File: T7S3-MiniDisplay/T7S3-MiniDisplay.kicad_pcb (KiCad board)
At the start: 2 copper layers, 67.3 x 63.5 mm, 30 parts, among them J101 Qwicc, J102 Micro_SD_Card_Det, J801 RJ45, J802 RJ45, T801 - 15 in +, T802 - 15 out +, U101 TTGO-T7_S3-V1.1, U301 AP63205, U801 TCAN332DR

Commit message: Minor updates.
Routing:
- net /SDA: track 57.0 -> 49.8 mm
- net /SCL: track 65.3 -> 62.5 mm
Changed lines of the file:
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@@
   (segment (start 108.877 91.1255) (end 108.959 91.2075) (width 0.8) (layer "F.Cu") (net 35))
   (segment (start 108.877 84.582) (end 108.877 91.1255) (width 0.8) (layer "F.Cu") (net 35))
-  (segment (start 103.025685 53.914) (end 103.632 53.307685) (width 0.2) (layer "F.Cu") (net 36))
-  (segment (start 103.632 53.307685) (end 103.632 50.0595) (width 0.2) (layer "F.Cu") (net 36))
+  (segment (start 103.632 53.307685) (end 103.025685 53.914) (width 0.2) (layer "F.Cu") (net 36))
   (segment (start 123.698 52.07) (end 123.698 37.338) (width 0.2) (layer "F.Cu") (net 36))
+  (segment (start 103.632 52.07) (end 103.632 53.307685) (width 0.2) (layer "F.Cu") (net 36))
   (segment (start 123.698 37.338) (end 123.444 37.084) (width 0.2) (layer "F.Cu") (net 36))
-  (segment (start 102.87 53.914) (end 103.025685 53.914) (width 0.2) (layer "F.Cu") (net 36))
+  (segment (start 103.025685 53.914) (end 102.87 53.914) (width 0.2) (layer "F.Cu") (net 36))
   (segment (start 102.796 53.84) (end 102.87 53.914) (width 0.2) (layer "F.Cu") (net 36))
   (segment (start 101.06 53.84) (end 102.796 53.84) (width 0.2) (layer "F.Cu") (net 36))
   (via (at 123.444 37.084) (size 0.8) (drill 0.4) (layers "F.Cu" "B.Cu") (net 36))
   (via (at 123.698 52.07) (size 0.8) (drill 0.4) (layers "F.Cu" "B.Cu") (net 36))
-  (via (at 103.632 50.0595) (size 0.8) (drill 0.4) (layers "F.Cu" "B.Cu") (net 36))
+  (via (at 103.632 52.07) (size 0.8) (drill 0.4) (layers "F.Cu" "B.Cu") (net 36))
   (segment (start 123.698 36.83) (end 144.78 36.83) (width 0.2) (layer "B.Cu") (net 36))
   (segment (start 144.78 36.83) (end 146.05 35.56) (width 0.2) (layer "B.Cu") (net 36))
   (segment (start 123.444 37.084) (end 123.698 36.83) (width 0.2) (layer "B.Cu") (net 36))
-  (segment (start 103.632 50.0595) (end 105.6425 52.07) (width 0.2) (layer "B.Cu") (net 36))
-  (segment (start 105.6425 52.07) (end 123.698 52.07) (width 0.2) (layer "B.Cu") (net 36))
-  (segment (start 98.552 53.34) (end 100.052 54.84) (width 0.2) (layer "F.Cu") (net 37))
+  (segment (start 103.632 52.07) (end 123.698 52.07) (width 0.2) (layer "B.Cu") (net 36))
+  (segment (start 105.300767 49.36) (end 105.300767 52.530233) (width 0.2) (layer "F.Cu") (net 37))
+  (segment (start 105.300767 52.530233) (end 102.87 54.961) (width 0.2) (layer "F.Cu") (net 37))
   (segment (start 101.06 54.84) (end 102.749 54.84) (width 0.2) (layer "F.Cu") (net 37))
-  (segment (start 98.722 49.36) (end 98.552 49.53) (width 0.2) (layer "F.Cu") (net 37))
   (segment (start 102.749 54.84) (end 102.87 54.961) (width 0.2) (layer "F.Cu") (net 37))
-  (segment (start 100.052 54.84) (end 101.06 54.84) (width 0.2) (layer "F.Cu") (net 37))
-  (segment (start 98.552 49.53) (end 98.552 53.34) (width 0.2) (layer "F.Cu") (net 37))
-  (via (at 98.722 49.36) (size 0.8) (drill 0.4) (layers "F.Cu" "B.Cu") (net 37))
+  (via (at 105.300767 49.36) (size 0.8) (drill 0.4) (layers "F.Cu" "B.Cu") (net 37))
+  (segment (start 105.300767 49.36) (end 144.61 49.36) (width 0.2) (layer "B.Cu") (net 37))
   (segment (start 144.61 49.36) (end 146.05 50.8) (width 0.2) (layer "B.Cu") (net 37))
-  (segment (start 98.722 49.36) (end 144.61 49.36) (width 0.2) (layer "B.Cu") (net 37))
   (segment (start 114.249487 33.788513) (end 114.134 33.904) (width 0.2) (layer "F.Cu") (net 38))
   (segment (start 116.332 36.322) (end 116.332 35.052) (width 0.2) (layer "F.Cu") (net 38))

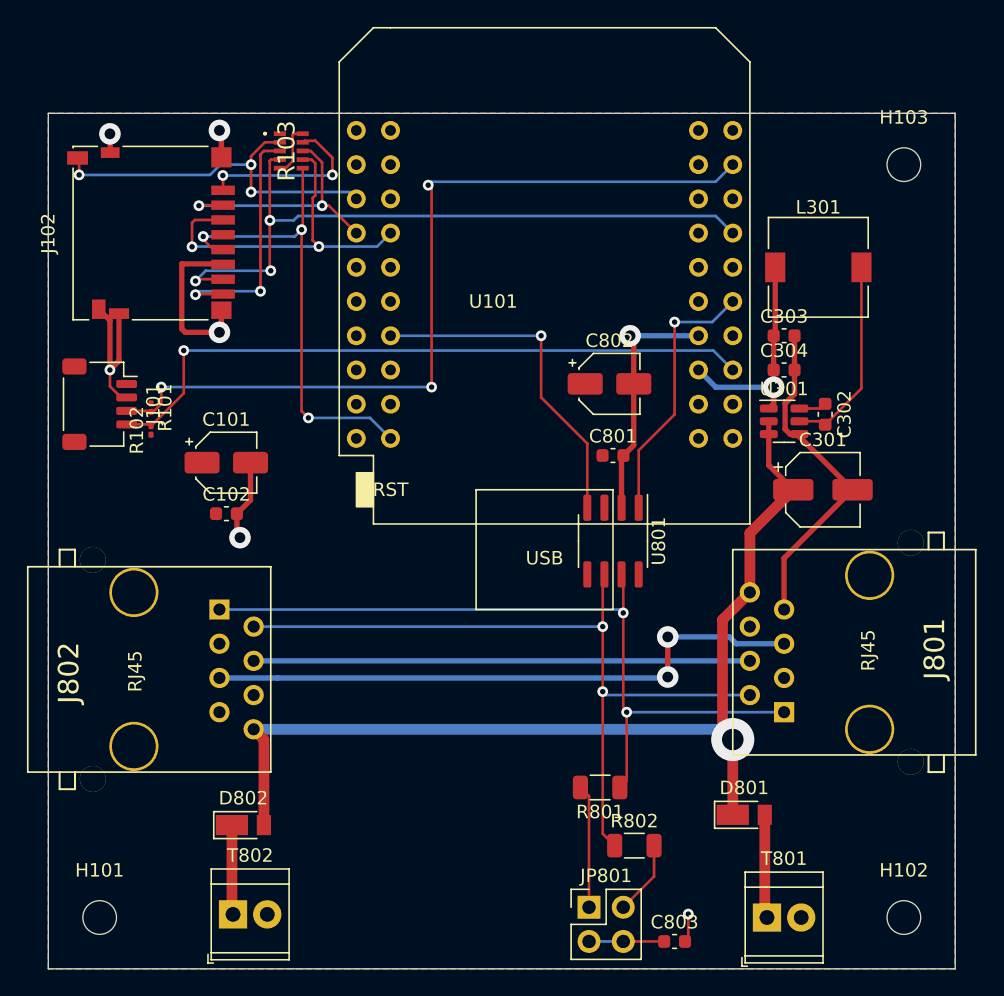
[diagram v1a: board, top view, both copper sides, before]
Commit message: Clean up PCB silkscreen.
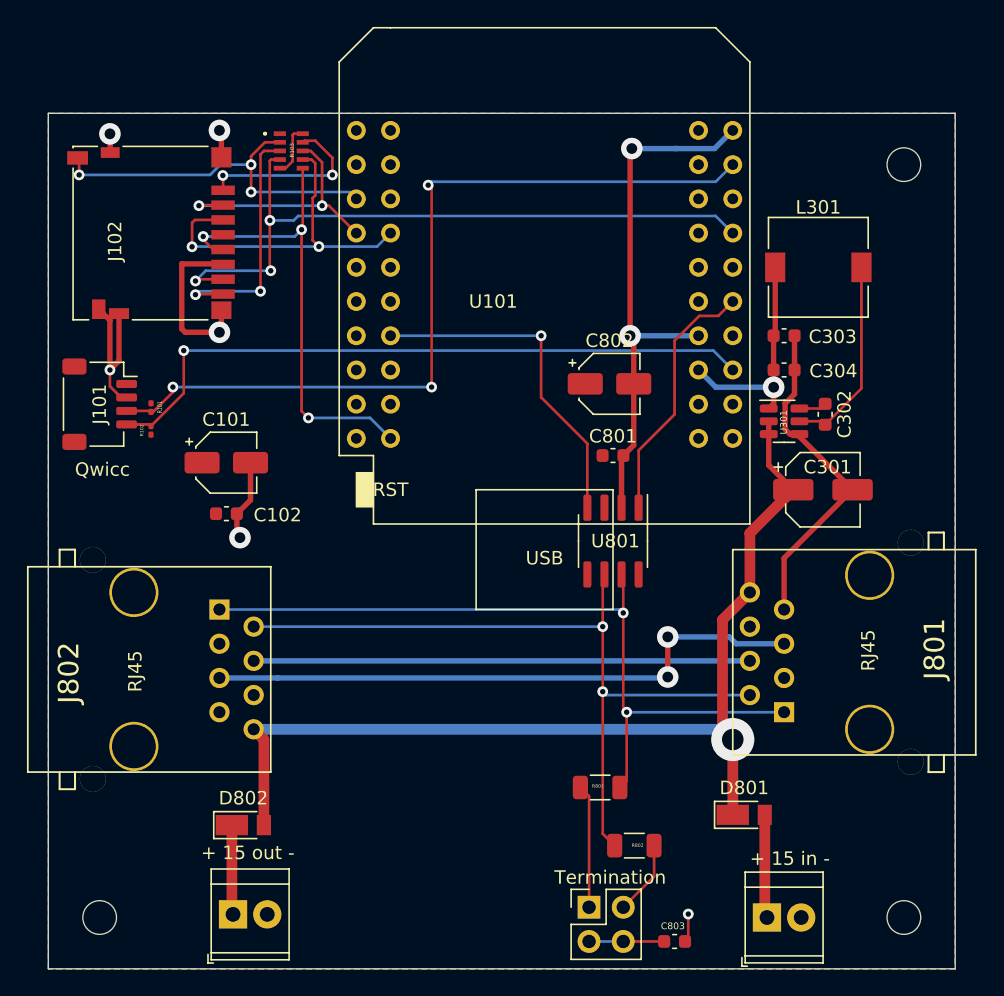
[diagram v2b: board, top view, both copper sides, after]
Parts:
- T801: value - 15 in + -> + 15 in -
- T802: value - 15 out + -> + 15 out -
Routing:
- net GND: track 79.8 -> 102.1 mm, vias 7 -> 8
- net /CAN Tx: track 19.8 -> 19.0 mm, vias 1 -> 0
- net /SCL: track 62.5 -> 62.0 mm

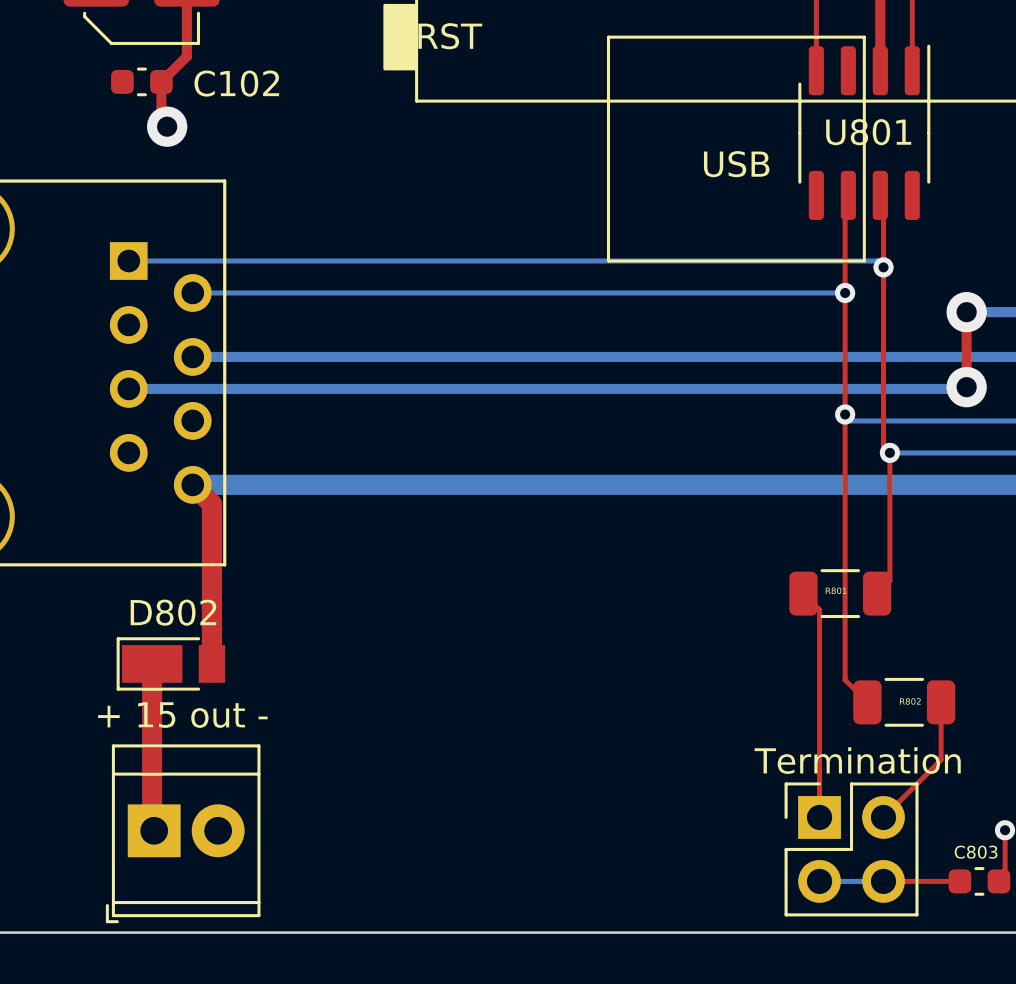
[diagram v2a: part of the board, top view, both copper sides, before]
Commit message: Clean up PCB silkscreen.
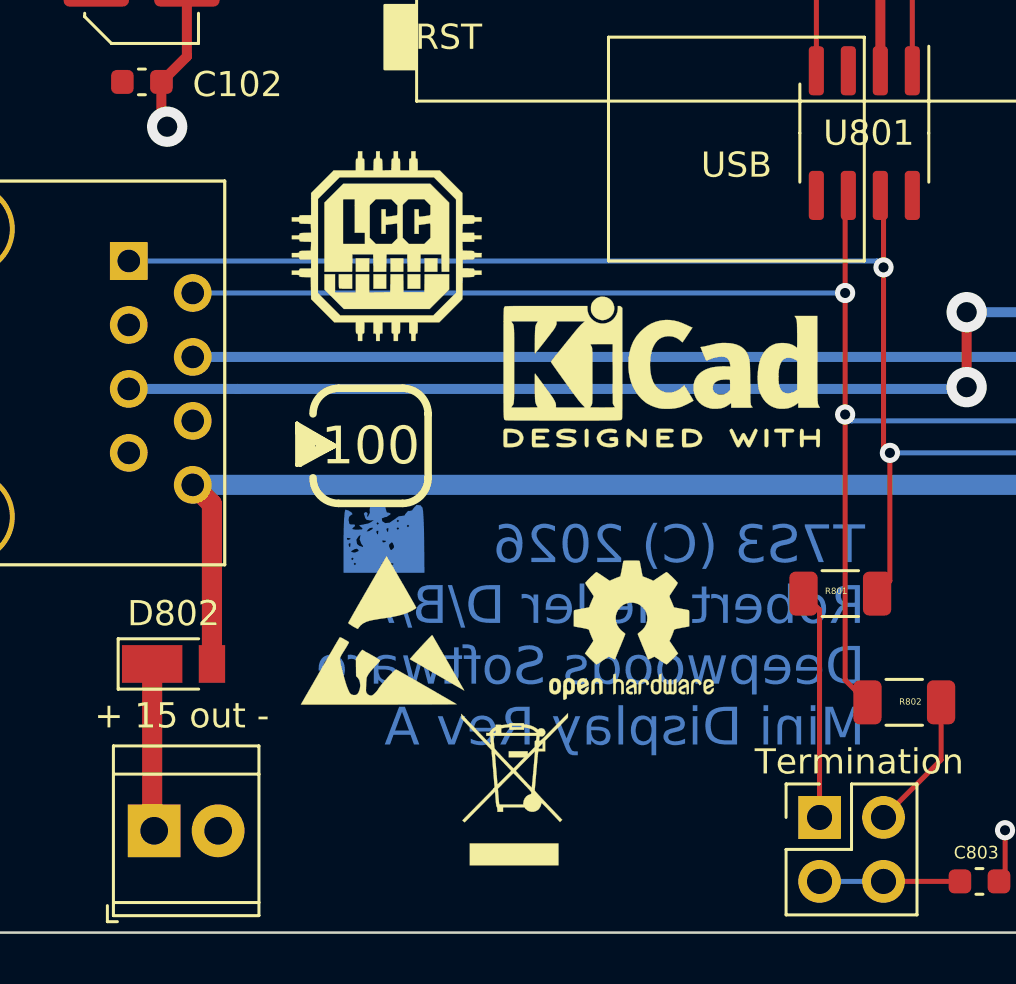
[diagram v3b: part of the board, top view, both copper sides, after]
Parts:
- added G***: LOGO, DWSLogo:DWSLogoBCU, F.Cu at (118.1, 79.4)
- added G***: LCC, LCC-Logo:LCC_LOGO_9x9, F.Cu at (118.2, 67.9)
- added REF**: WEEE-Logo_4.2x6mm_SilkScreen, Symbol:WEEE-Logo_4.2x6mm_SilkScreen, F.Cu at (123.3, 89.6)
- added REF**: KiCad-Logo2_5mm_SilkScreen, Symbol:KiCad-Logo2_5mm_SilkScreen, F.Cu at (129.1, 73.0)
- added REF**: ESD-Logo_6.6x6mm_SilkScreen, Symbol:ESD-Logo_6.6x6mm_SilkScreen, F.Cu at (118.0, 83.2)
- added REF**: OSHW-Logo2_7.3x6mm_SilkScreen, Symbol:OSHW-Logo2_7.3x6mm_SilkScreen, F.Cu at (127.9, 83.2)
- added REF**: PowerLabel-100, Power:PowerLabel-100, F.Cu at (117.6, 75.9)
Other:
- board text added: "T7S3 (C) 2026 Robert Heller D/B/A Deepwoods Software Mini Display Rev A"

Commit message: Finalize part numbers.
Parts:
- J101: footprint Connector_JST:JST_SH_SM04B-SRSS-TB_1x04-1MP_P1.00mm_Horizontal -> Connector_JST:JST_PH_S4B-PH-SM4-TB_1x04-1MP_P2.00mm_Horizontal
- moved R102 4.71 mm to (106.5, 58.3)
- moved R101 4.03 mm to (106.5, 55.4)
- moved C101 2.65 mm to (111.1, 57.9)
- moved C102 2.65 mm to (111.1, 61.6)
- moved J101 1.96 mm to (100.2, 54.9)
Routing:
- net GND: track 102.1 -> 108.7 mm
- net /SDA: track 49.8 -> 50.8 mm
